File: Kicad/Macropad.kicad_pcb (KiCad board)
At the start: 4 copper layers, 100 x 100 mm, 86 parts, among them J1 UJ20-C-H-G-SMT-5-P16-TR, SW1 SW_SPST, SW10 SW_SPST, SW11 SW_SPST, SW12 SW_SPST, SW13 SW_SPST, SW14 SW_SPST, SW15 SW_SPST, SW16 SW_SPST, SW17 SW_SPST, SW18 SW_SPST, SW19 SW_SPST, SW2 SW_SPST, SW20 SW_SPST, SW21 SW_SPST, SW22 SW_SPST, SW23 SW_SPST, SW24 SW_SPST, SW25 SW_SPST, SW26 SW_Reset, SW27 SW_HWB, SW3 SW_SPST, SW4 SW_SPST, SW5 SW_SPST, SW6 SW_SPST, SW7 SW_SPST, SW8 SW_SPST, SW9 SW_SPST, U1 ATmega32U4-A, Y1 LFXTAL085842

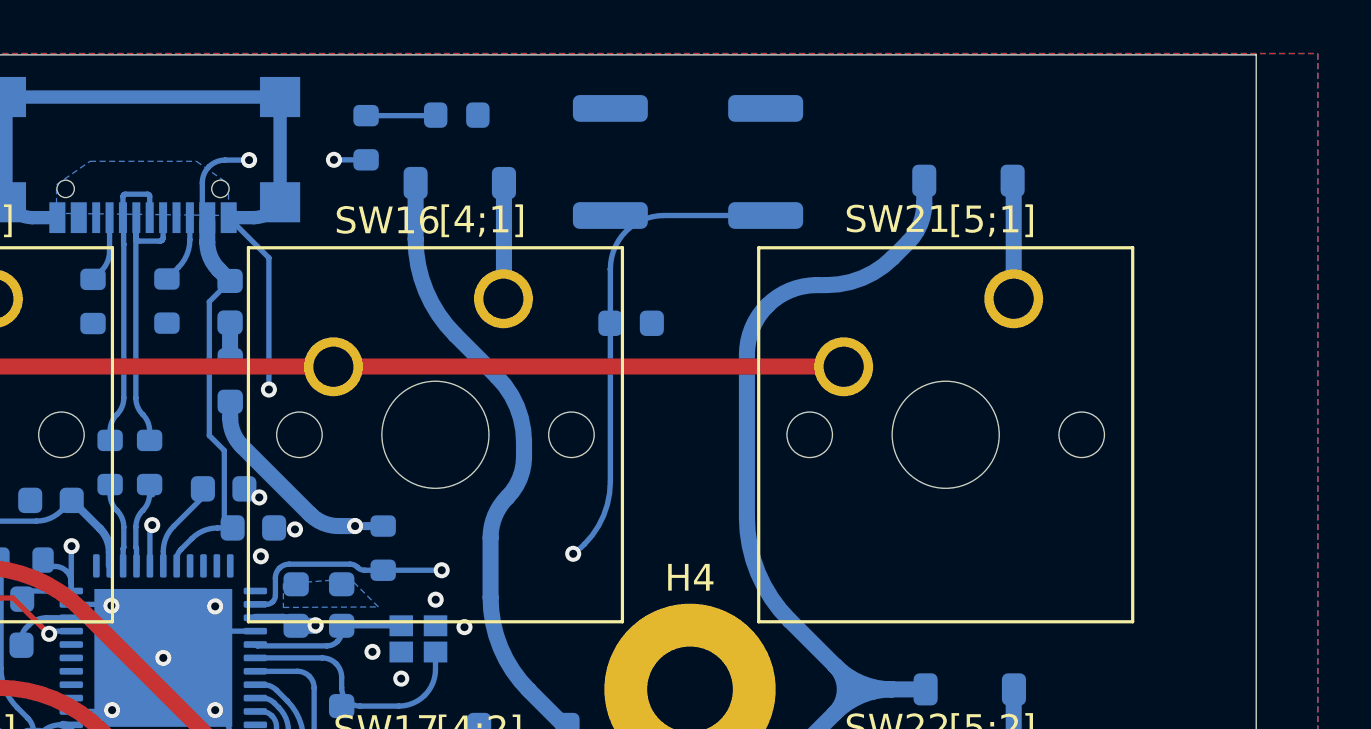
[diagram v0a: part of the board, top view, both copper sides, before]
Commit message: added debug pins
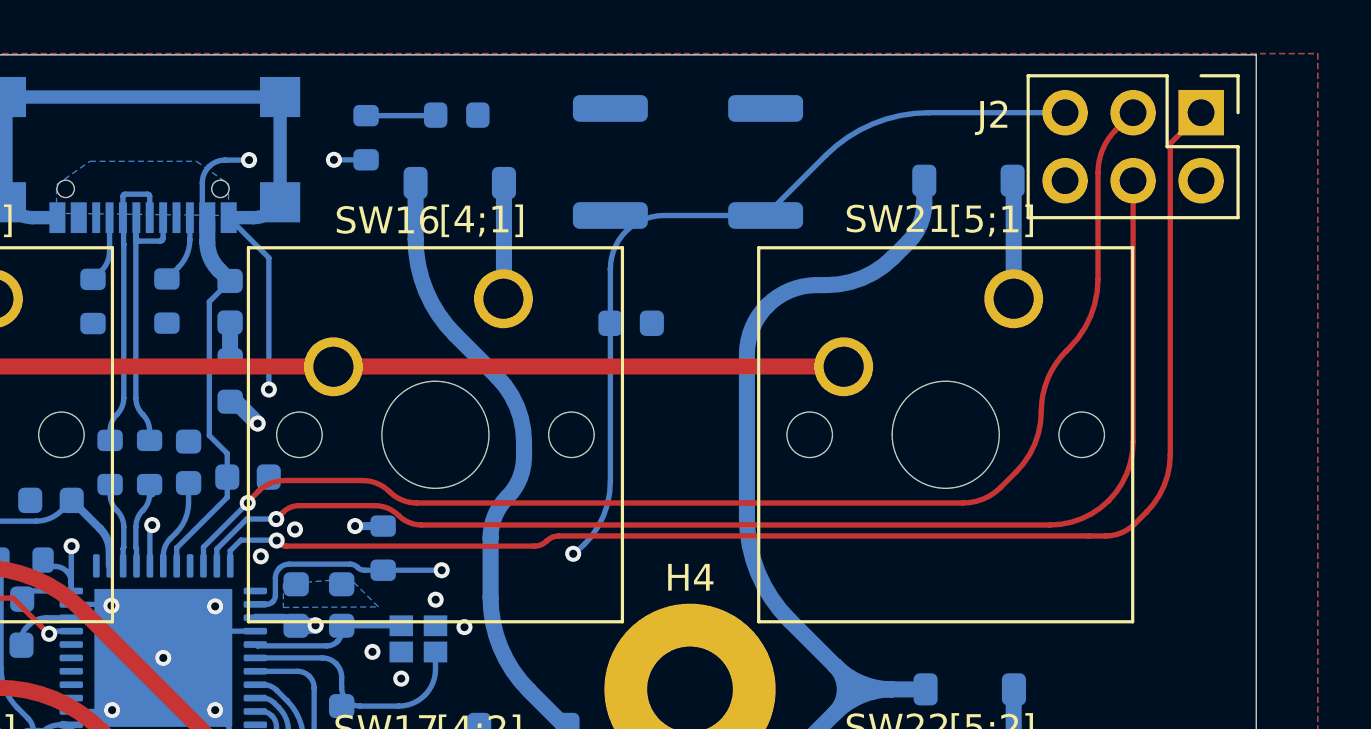
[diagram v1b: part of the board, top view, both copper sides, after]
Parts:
- added J2: Conn_01x06_Pin, Connector_PinHeader_2.54mm:PinHeader_2x03_P2.54mm_Vertical, F.Cu at (114.0, 17.4)
- moved C8 1.91 mm to (78.4, 31.0)
- moved C1 1.64 mm to (76.2, 30.4), turned to 90 degrees
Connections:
- net Net-(U1-~{RESET}) renamed RESET
- U1 pad 10: unconnected-(U1-PB2-Pad10) -> MOSI
- U1 pad 11: unconnected-(U1-PB3-Pad11) -> MISO
- U1 pad 9: unconnected-(U1-PB1-Pad9) -> SCK
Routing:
- net MISO: track 0.00 -> 51.0 mm, vias 0 -> 1
- net SCK: track 0.00 -> 47.3 mm, vias 0 -> 1
- net MOSI: track 0.00 -> 47.2 mm, vias 0 -> 1
- net +5V: track 41.8 -> 83.9 mm, vias 3 -> 4
- net RESET: track 31.2 -> 43.7 mm
- net uGND: track 37.2 -> 38.5 mm
- net VBUS: track 23.4 -> 22.7 mm
- net Net-(C11-Pad1): track 23.7 -> 24.4 mm
- net GND: vias 16 -> 15
